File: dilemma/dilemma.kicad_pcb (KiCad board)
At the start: 2 copper layers, 154.5 x 108.7 mm, 91 parts, among them J1 S3B-PH-SM4-TB(LF)(SN), J2 Serial, J3 BATTERY_CONN_DEANS, J5 S3B-PH-SM4-TB(LF)(SN), SW1 SW_Push, SW10 SW_Push, SW11 SW_Push, SW12 SW_Push, SW13 SW_Push, SW14 SW_Push, SW15 SW_Push, SW16 SW_Push, SW17 locked, SW18 SW_Push, SW19 SW_Push, SW2 SW_Push, SW20 SW_Push, SW21 SW_Push, SW26 SW_SPST, SW3 SW_Push, SW37 SW_SPST, SW4 SW_Push, SW5 SW_Push, SW6 SW_Push, SW7 SW_Push, SW8 SW_Push, SW9 SW_Push, U2 eliteC

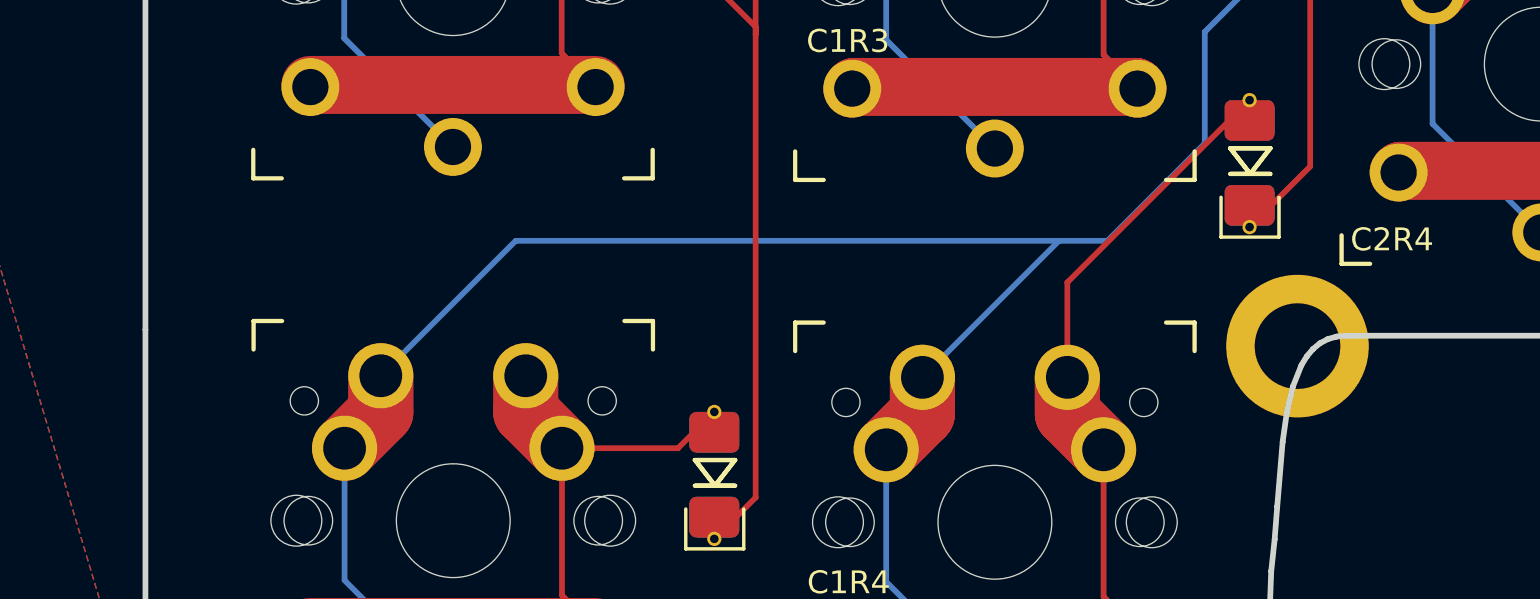
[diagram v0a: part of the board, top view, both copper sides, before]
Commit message: Move mounting hole to the left
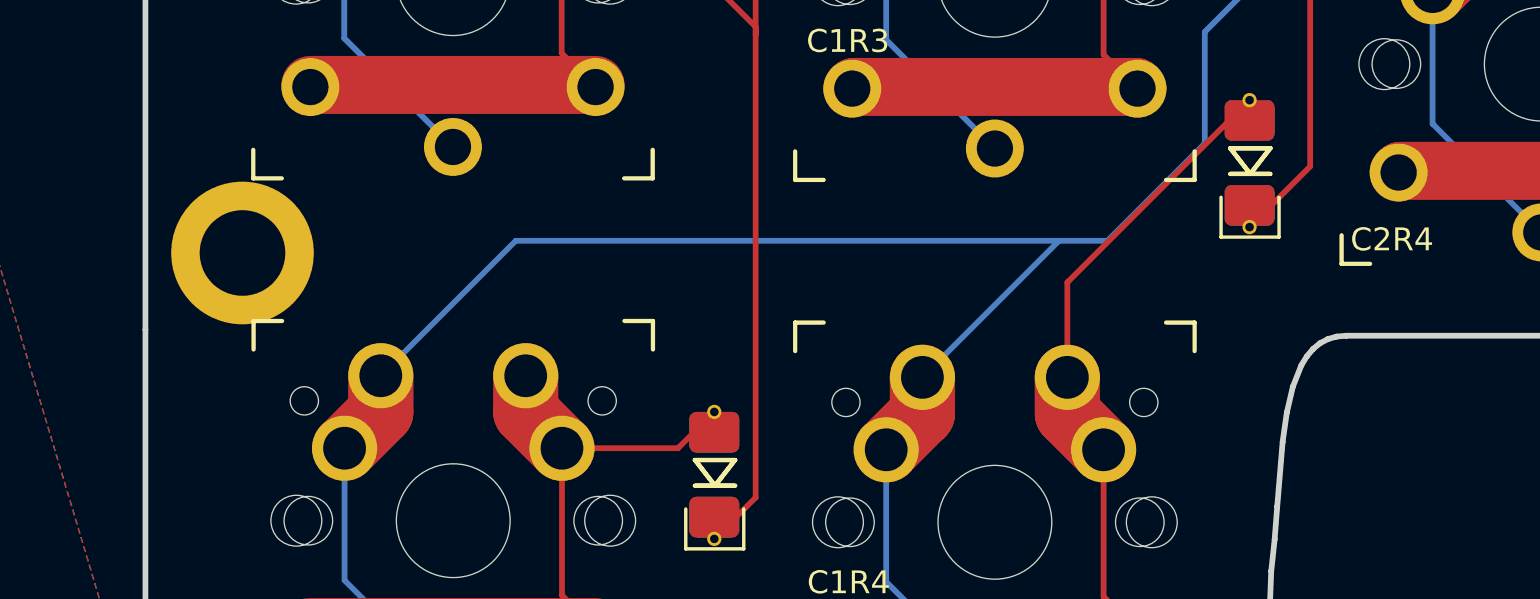
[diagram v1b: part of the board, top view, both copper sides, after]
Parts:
- moved H4 37.1 mm to (88.9, 83.8)

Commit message: Update slik screen layer
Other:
- board text added: "BastardKB x Freznel x ghostbuster91"
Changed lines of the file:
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@@
     (effects (font (size 0.8 0.8) (thickness 0.12)))
   )
-  (gr_text "R4" (at 230.788472 53.536876) (layer "F.SilkS")
+  (gr_text "C5" (at 230.788472 53.536876) (layer "F.SilkS")
     (effects (font (size 0.8 0.8) (thickness 0.12)))
   )
@@
     (effects (font (size 0.8 0.8) (thickness 0.12)))
   )
-  (gr_text "SC" (at 230.788472 56.100938) (layer "F.SilkS")
+  (gr_text "R1" (at 230.788472 56.100938) (layer "F.SilkS")
     (effects (font (size 0.8 0.8) (thickness 0.12)))
   )
@@
     (effects (font (size 0.8 0.8) (thickness 0.12)))
   )
-  (gr_text "C6" (at 230.788472 50.972814) (layer "F.SilkS")
+  (gr_text "R4" (at 230.788472 50.972814) (layer "F.SilkS")
     (effects (font (size 0.8 0.8) (thickness 0.12)))
   )
@@
     (effects (font (size 0.8 0.8) (thickness 0.12)))
   )
-  (gr_text "R1" (at 230.788472 48.408752) (layer "F.SilkS")
+  (gr_text "C6" (at 230.788472 48.408752) (layer "F.SilkS")
     (effects (font (size 0.8 0.8) (thickness 0.12)))
   )
@@
     (effects (font (size 0.8 0.8) (thickness 0.12)))
   )
-  (gr_text "BastardKB x Freznel" (at 206.75 49.25 90) (layer "F.SilkS")
+  (gr_text "BastardKB x Freznel\nx ghostbuster91" (at 207.75 49.425 90) (layer "F.SilkS")
     (effects (font (size 0.8 0.8) (thickness 0.12)))
   )
